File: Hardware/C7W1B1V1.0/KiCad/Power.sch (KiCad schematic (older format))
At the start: 36 parts, among them IC1 USBLC6-2P6, IC2 LMR62421XSD_NOPB, IC3 S-8261AAXMD-G2XT2U, J3 USB4105GFA120, J4 Conn_01x02_Male, Q1 PMDPB30XNAX, U3 STC4054GR

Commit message: Dodano projekt Cube
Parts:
- added C21: 10n/16V/X5R, Capacitor_SMD:C_0402_1005Metric, symbol Device:C
- renumbered C20 to C13, C21 to C14, C11 to C15, C12 to C16, C22 to C17, C13 to C18, C14 to C19, C15 to C20, C16 to C22, C17 to C23, C23 to C24, C18 to C25, J3 to J2, J4 to J3, R14 to R12, R15 to R13, R9 to R14, R16 to R15, R17 to R16, R10 to R17, R11 to R18, R18 to R19, R12 to R20, R13 to R21, R19 to R22, R20 to R23, R21 to R24, U3 to U5
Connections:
- net 5V_TEST: now also C21.1
- net GND: now also C21.2
- net VBUS: no longer C13.1, F1.2, J2.A4_B9 (VBUS), J2.B4_A9 (VBUS__1)
- new net USB_VBUS: C13.1, F1.2, J2.A4_B9 (VBUS), J2.B4_A9 (VBUS__1)

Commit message: Ukończono PCB. dodano pliki produkcyjne
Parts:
- added C27, C28: 10u/6.3V/X5R, Capacitor_SMD:C_0402_1005Metric, symbol Device:C
- added R13: 0R, Resistor_SMD:R_0402_1005Metric, symbol Device:R
- added U9: LD39200PU33R, Footprints:SON95P300X300X100-7N-D, symbol LD39200PU33R:LD39200PU33R
- renumbered R13 to R14, R14 to R15, R15 to R16, R16 to R17, R17 to R18, R18 to R19, R19 to R20, R20 to R21, R21 to R22, R22 to R23, R23 to R24, R24 to R25, IC1 to U5, U5 to U6, IC2 to U7, IC3 to U8
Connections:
- net +3V3: now also C27.1, U9.1 (OUT), U9.2 (ADJ/SENSE)
- net +BATT: now also C28.1, U9.5 (EN), U9.6 (IN)
- net GND: now also C19.2, C20.2, C22.2, C23.2, C25.2, C27.2, C28.2, R13.1, U9.3 (GND), U9.7 (EPAD)
- net GND1: now also R13.2
- no-connect marks 2 -> 3
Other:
- note added: "You can solder R13 if the battery has its own protection.\n In this case, you do not need to solder U8 and Q1 and their associated components"

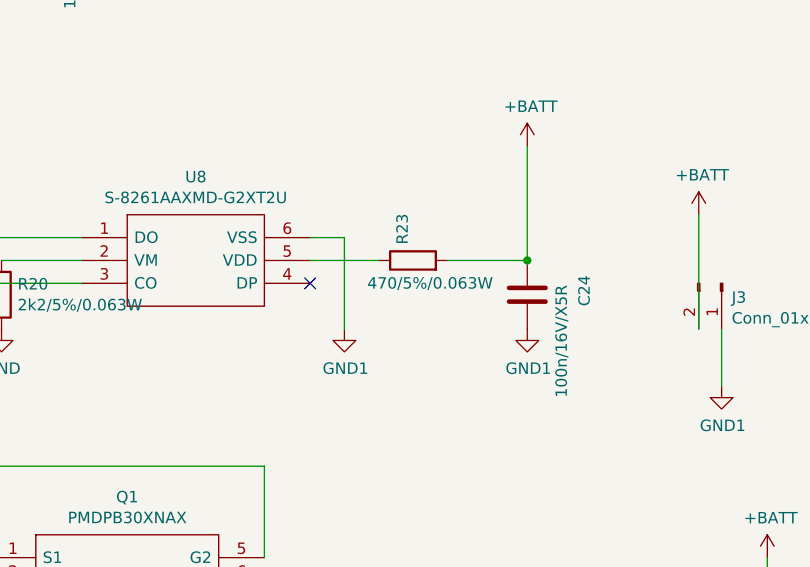
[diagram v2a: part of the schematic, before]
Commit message: Zmieniono procesor na wersję LQFP-64
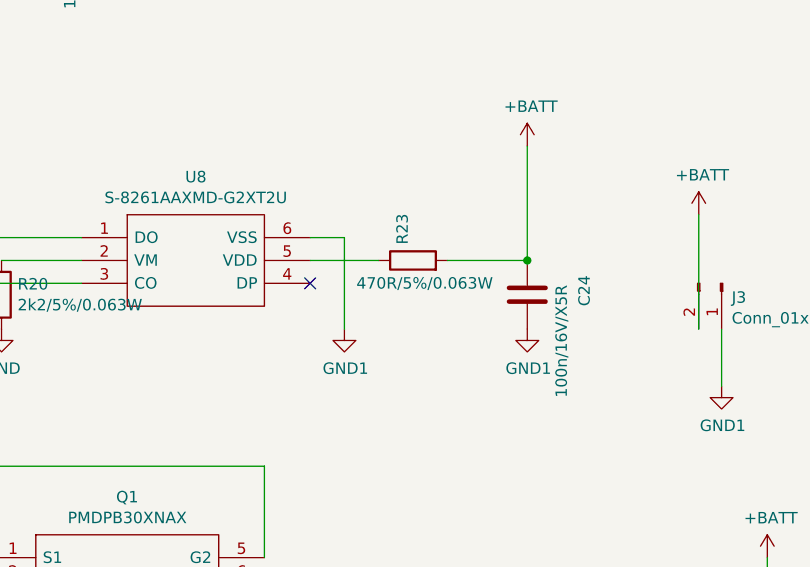
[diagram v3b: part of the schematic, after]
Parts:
- R23: value 470/5%/0.063W -> 470R/5%/0.063W
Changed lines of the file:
@@
 AR Path="/672E4E38/673C97CB" Ref="R23"  Part="1"
 F 0 "R23" H 13870 4146 50  0000 L CNN
-F 1 "470/5%/0.063W" V 13700 3750 50  0000 L CNN
+F 1 "470R/5%/0.063W" V 13700 3750 50  0000 L CNN
 F 2 "Resistor_SMD:R_0402_1005Metric" V 13730 4100 50  0001 C CNN
 F 3 "~" H 13800 4100 50  0001 C CNN
